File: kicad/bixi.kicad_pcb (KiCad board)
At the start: 2 copper layers, 87.5 x 100 mm, 38 parts, among them J1 RJ45, J2 RJ45, J3 RJ45, J4 RJ45, J5 RJ45, J6 RJ45, J7 RJ45, J8 RJ45, J9 Screw_Terminal_1x02, U1 Teensy3.6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

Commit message: keep-out area for terminal block, finalized node pcb
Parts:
- moved J9 3.00 mm to (172.0, 95.0)
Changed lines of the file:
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@@
       (net 46 "Net-(J8-Pad2)"))
-  )
-  (module custom:HB9500-2P (layer F.Cu)
-    (at 175 95 90)
-    (fp_text reference J9 (at 0 0.5 90) (layer F.SilkS)
-      (effects (font (size 1 1) (thickness 0.15)))
-    )
-    (fp_text value Screw_Terminal_1x02 (at 0 -0.5 90) (layer F.Fab)
-      (effects (font (size 1 1) (thickness 0.15)))
-    )
-    (pad 1 thru_hole circle (at -5 0 90) (size 1.524 1.524) (drill 0.762) (layers *.Cu *.Mask)
-      (net 1 VCC))
-    (pad 2 thru_hole circle (at 4.5 0 90) (size 1.524 1.524) (drill 0.762) (layers *.Cu *.Mask)
-      (net 2 GND))
   )
   (module Mounting_Holes:MountingHole_3.5mm_Pad (layer F.Cu)
@@
     (pad 1 thru_hole circle (at 0 0) (size 7 7) (drill 3.5) (layers *.Cu *.Mask))
   )
+  (module custom:HB9500-2P (layer F.Cu)
+    (at 172 95 90)
+    (fp_text reference J9 (at 0 0.5 90) (layer F.SilkS)
+      (effects (font (size 1 1) (thickness 0.15)))
+    )
+    (fp_text value Screw_Terminal_1x02 (at 0 -0.5 90) (layer F.Fab)
+      (effects (font (size 1 1) (thickness 0.15)))
+    )
+    (fp_line (start -9.5 -8) (end 9.5 -8) (layer F.SilkS) (width 0.15))
+    (fp_line (start 9.5 -8) (end 9.5 8) (layer F.SilkS) (width 0.15))
+    (fp_line (start 9.5 8) (end -9.5 8) (layer F.SilkS) (width 0.15))
+    (fp_line (start -9.5 8) (end -9.5 -8) (layer F.SilkS) (width 0.15))
+    (pad 1 thru_hole circle (at -4.75 0 90) (size 1.524 1.524) (drill 0.762) (layers *.Cu *.Mask)
+      (net 1 VCC))
+    (pad 2 thru_hole circle (at 4.75 0 90) (size 1.524 1.524) (drill 0.762) (layers *.Cu *.Mask)
+      (net 2 GND))
+  )
   (gr_line (start 95 55) (end 95 135) (angle 90) (layer Edge.Cuts) (width 0.15))

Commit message: larger pads on screw terminal connector
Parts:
- moved J9 2.00 mm to (170.0, 95.0)
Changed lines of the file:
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@@
     (links 106)
     (no_connects 0)
-    (area 90.085714 42.5 184.914286 147.500001)
+    (area 94.924999 44.924999 182.575001 145.075001)
     (thickness 1.6)
     (drawings 8)
@@
     (pcbplotparams
       (layerselection 0x00030_80000001)
-      (usegerberextensions false)
+      (usegerberextensions true)
       (excludeedgelayer true)
       (linewidth 0.100000)
@@
       (outputformat 1)
       (mirror false)
-      (drillshape 1)
+      (drillshape 0)
       (scaleselection 1)
       (outputdirectory ""))
@@
   )
   (module custom:HB9500-2P (layer F.Cu)
-    (at 172 95 90)
+    (at 170 95 90)
     (fp_text reference J9 (at 0 0.5 90) (layer F.SilkS)
       (effects (font (size 1 1) (thickness 0.15)))
@@
     (fp_line (start 9.5 8) (end -9.5 8) (layer F.SilkS) (width 0.15))
     (fp_line (start -9.5 8) (end -9.5 -8) (layer F.SilkS) (width 0.15))
-    (pad 1 thru_hole circle (at -4.75 0 90) (size 1.524 1.524) (drill 0.762) (layers *.Cu *.Mask)
-      (net 1 VCC))
-    (pad 2 thru_hole circle (at 4.75 0 90) (size 1.524 1.524) (drill 0.762) (layers *.Cu *.Mask)
-      (net 2 GND))
-  )
+    (pad 1 thru_hole circle (at -4.75 0 90) (size 2.6 2.6) (drill 1.3) (layers *.Cu *.Mask)
+      (net 1 VCC))
+    (pad 2 thru_hole circle (at 4.75 0 90) (size 2.6 2.6) (drill 1.3) (layers *.Cu *.Mask)
+      (net 2 GND))
+  )

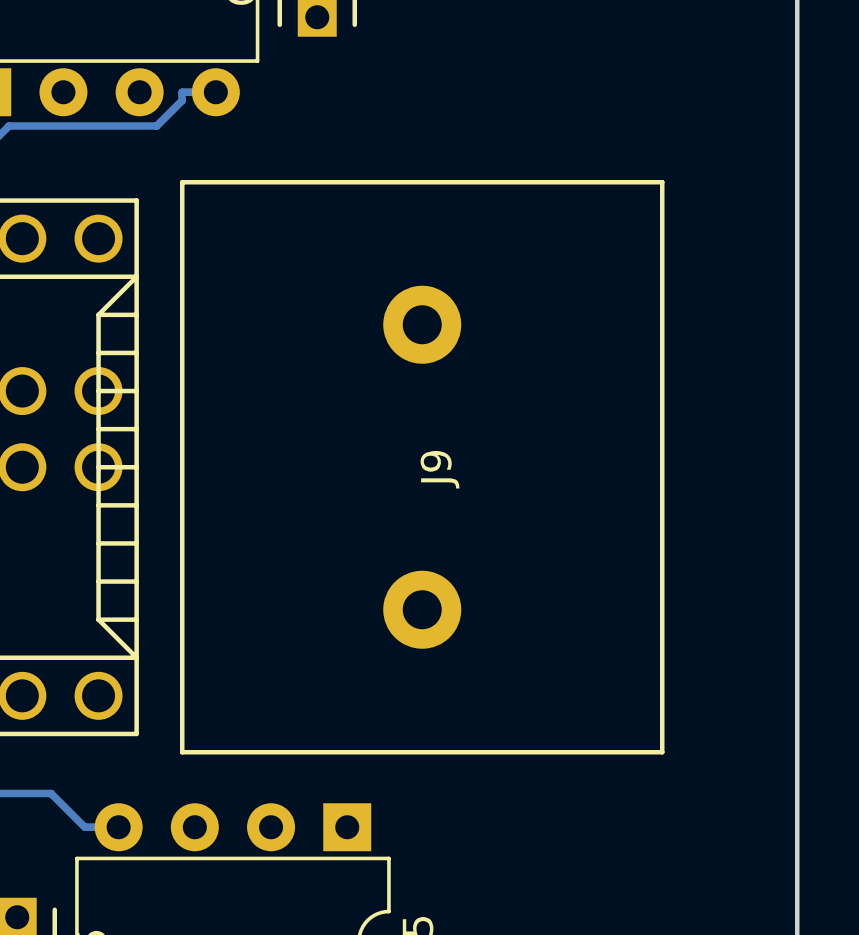
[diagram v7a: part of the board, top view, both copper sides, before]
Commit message: both pcb's sent to fab
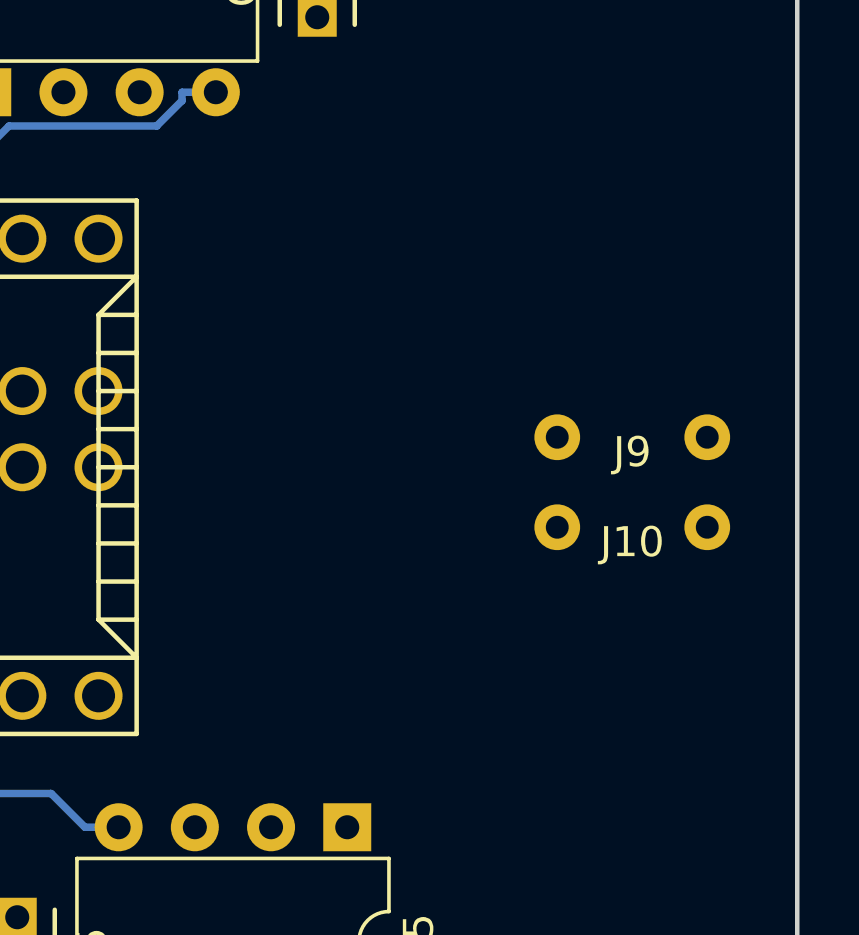
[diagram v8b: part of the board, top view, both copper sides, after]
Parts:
- added J10: Screw_Terminal_1x01, custom:A116169CT_SPADE_CONNECTOR, F.Cu at (177.0, 97.0)
- added bm_streets: , logos:bm_streets, F.Cu at (91.0, 54.0)
- J9: value Screw_Terminal_1x02 -> Screw_Terminal_1x01; footprint custom:HB9500-2P -> custom:A116169CT_SPADE_CONNECTOR
- moved J9 7.07 mm to (177.0, 94.0), turned to 0 degrees
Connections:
- J9 pad 2: GND -> (no net)
